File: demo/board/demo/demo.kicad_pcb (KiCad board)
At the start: 2 copper layers, 25 parts, among them J2 Conn_01x20, J3 Conn_01x20, J6 FTSH-107-01-F-DV-K, U1 STM32F413CGUx, U2 LD1117S33TR_SOT223, U4 MAX33054EASA+T, Y1 CSTNE8M00

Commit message: finished demo board schem and layout
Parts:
- J2, J3: moved to B.Cu
- R1: moved to F.Cu
- moved R1 10.1 mm to (151.9, 99.7), turned to 180 degrees
- moved D2 9.04 mm to (155.4, 99.7)
- moved C7 4.38 mm to (152.6, 98.3), turned to 0 degrees
- moved C4 4.28 mm to (149.0, 96.6), turned to 180 degrees
- moved R10 3.61 mm to (151.6, 72.6), turned to 180 degrees
- moved C2 2.19 mm to (147.9, 107.6)
- moved C3 2.04 mm to (149.7, 107.6)
- moved C9 1.72 mm to (147.2, 87.2), turned to 90 degrees
- moved C11 1.60 mm to (158.9, 95.0)
- moved C5 1.43 mm to (148.7, 84.9), turned to 90 degrees
- moved Y1 1.17 mm to (151.3, 82.6)
- moved R6 0.90 mm to (148.8, 63.1), turned to 180 degrees
- moved J6 0.79 mm to (153.2, 73.7), turned to -90 degrees
- moved C10 0.69 mm to (155.1, 84.1)
- moved JP1 0.53 mm to (153.8, 82.0)
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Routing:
- net +3V3: track 0.00 -> 111.2 mm, vias 0 -> 8
- net A11: track 0.00 -> 45.0 mm, vias 0 -> 1
- net A12: track 0.00 -> 40.7 mm, vias 0 -> 1
- net B3_TRACESWO: track 0.00 -> 32.6 mm, vias 0 -> 1
- net B9: track 0.00 -> 31.3 mm
- net C13: track 0.00 -> 29.1 mm
- net B8: track 0.00 -> 29.0 mm
- net B7: track 0.00 -> 26.9 mm
- net A13_SWDIO: track 0.00 -> 26.4 mm, vias 0 -> 1
- net B6: track 0.00 -> 24.5 mm
- net A14_SWCLK: track 0.00 -> 24.4 mm, vias 0 -> 1
- net B5: track 0.00 -> 22.2 mm
- net C14: track 0.00 -> 21.1 mm
- net B4: track 0.00 -> 19.8 mm
- net C15: track 0.00 -> 18.8 mm
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- added copper zone on B.Cu, net GND
- added copper zone on F.Cu, net GND
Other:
- board outline added: 21.9 x 51.8 mm

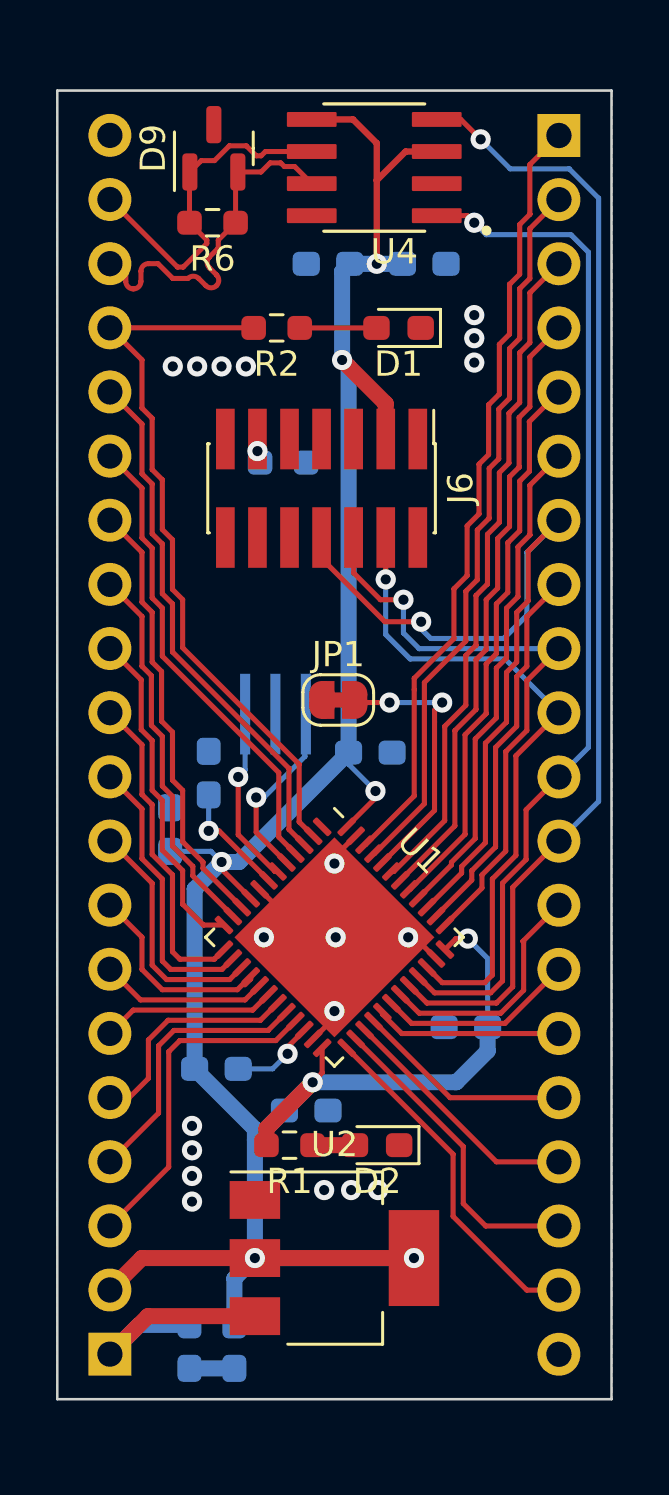
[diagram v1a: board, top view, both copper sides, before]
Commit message: finishing layout and labels
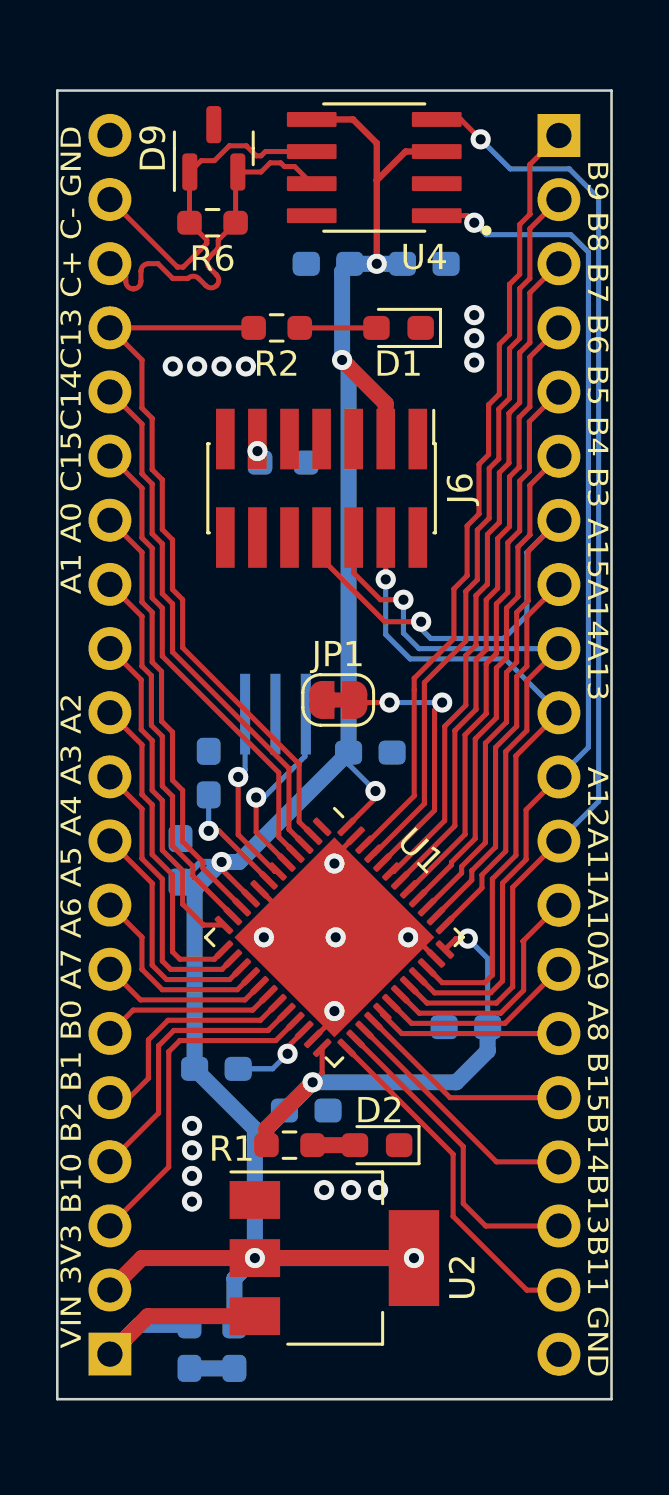
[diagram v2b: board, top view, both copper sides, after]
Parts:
- added G***: LOGO, AERO_Footprints:AERO_Logo_10x4mm, B.Cu at (153.7, 101.9)
- moved C9 1.29 mm to (147.6, 88.4)
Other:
- board text added: "A1 A0 C15C14C13 C+ C- GND"
- board text added: "A12A11A10A9 A8 B15B14B13B11 GND"
- board text added: "B9 B8 B7 B6 B5 B4 B3 A15A14A13"
- board text added: "G.Spearing STM32F413cgu"
- board text added: "VIN 3V3 B10 B2 B1 B0 A7 A6 A5 A4 A3 A2"
